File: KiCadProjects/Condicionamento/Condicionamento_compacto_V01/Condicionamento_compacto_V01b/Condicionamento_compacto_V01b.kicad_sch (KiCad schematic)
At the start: 19 parts, among them J1 Entrada, J2 Canais, J3 Conn_01x02, J4 Conn_01x02, U1-Cond1 AD8056ARMZ

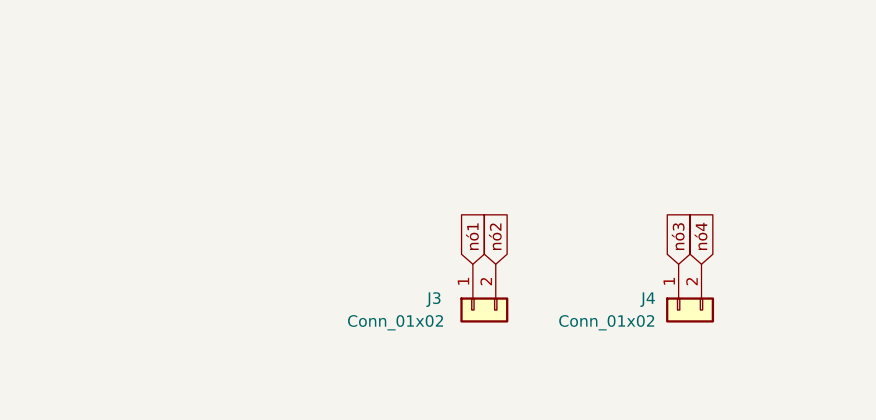
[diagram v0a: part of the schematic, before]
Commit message: V01aCopia: menor, com vias. V01a: maior, sem vias
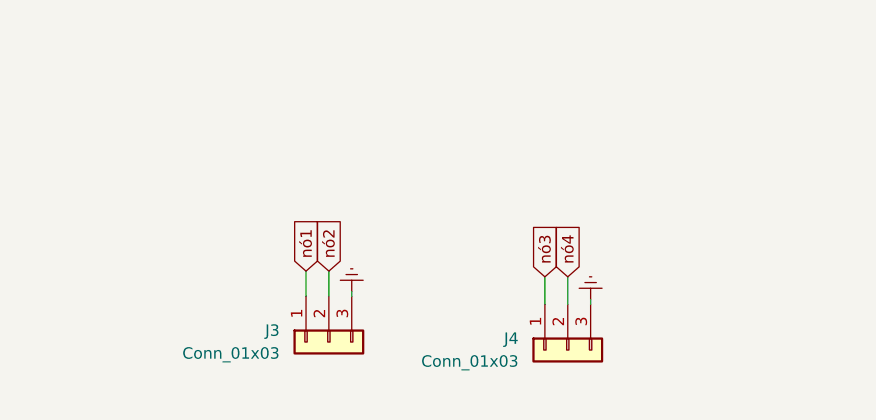
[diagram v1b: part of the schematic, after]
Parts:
- removed J3, J4: Conn_01x02, Connector_PinHeader_2.54mm:PinHeader_1x02_P2.54mm_Vertical, symbol Connector_Generic:Conn_01x02
- added J3, J4: Conn_01x03, Connector_PinHeader_2.54mm:PinHeader_1x03_P2.54mm_Vertical, symbol Connector_Generic:Conn_01x03
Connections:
- net Earth: now also J3.3 (Pin_3), J4.3 (Pin_3)
- net nó1: now also J3.1 (Pin_1)
- net nó2: now also J3.2 (Pin_2)
- net nó3: now also J4.1 (Pin_1)
- net nó4: now also J4.2 (Pin_2)
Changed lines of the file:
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@@
+    (stroke (width 0) (type default))
+  )
+  (wire (pts (xy 128.778 125.222) (xy 128.778 128.016))
     (stroke (width 0) (type default))
   )
@@
     (stroke (width 0) (type default))
   )
+  (wire (pts (xy 155.321 125.857) (xy 155.321 128.905))
+    (stroke (width 0) (type default))
+  )
   (wire (pts (xy 56.134 54.61) (xy 56.134 56.896))
     (stroke (width 0) (type default))
@@
     (stroke (width 0) (type default))
   )
+  (wire (pts (xy 152.781 125.857) (xy 152.781 128.905))
+    (stroke (width 0) (type default))
+  )
+  (wire (pts (xy 131.318 127.508) (xy 131.318 128.016))
+    (stroke (width 0) (type default))
+  )
   (wire (pts (xy 191.77 45.72) (xy 191.77 57.15))
     (stroke (width 0) (type default))
@@
     (stroke (width 0) (type default))
   )
+  (wire (pts (xy 126.238 125.222) (xy 126.238 128.016))
+    (stroke (width 0) (type default))
+  )
   (wire (pts (xy 96.52 54.61) (xy 96.52 65.532))
     (stroke (width 0) (type default))
@@
     (stroke (width 0) (type default))
   )
+  (wire (pts (xy 157.861 128.397) (xy 157.861 128.905))
+    (stroke (width 0) (type default))
+  )
   (wire (pts (xy 99.06 54.61) (xy 96.52 54.61))
     (stroke (width 0) (type default))
@@
     )
   )
+  (global_label "nó4" (shape input) (at 155.321 125.857 90) (fields_autoplaced)
+    (effects (font (size 1.27 1.27)) (justify left))
+    (property "Intersheetrefs" "${INTERSHEET_REFS}" (at 155.321 119.3643 90)
+      (effects (font (size 1.27 1.27)) (justify left) hide)
+    )
+  )
   (global_label "Vref" (shape input) (at 256.54 33.02 90) (fields_autoplaced)
     (effects (font (size 1.27 1.27)) (justify left))
@@
     )
   )
-  (global_label "nó2" (shape input) (at 147.32 124.46 90) (fields_autoplaced)
-    (effects (font (size 1.27 1.27)) (justify left))
-    (property "Intersheetrefs" "${INTERSHEET_REFS}" (at 147.32 117.9673 90)
-      (effects (font (size 1.27 1.27)) (justify left) hide)
-    )
-  )
-  (global_label "nó4" (shape input) (at 170.18 124.46 90) (fields_autoplaced)
-    (effects (font (size 1.27 1.27)) (justify left))
-    (property "Intersheetrefs" "${INTERSHEET_REFS}" (at 170.18 117.9673 90)
+  (global_label "nó1" (shape input) (at 126.238 125.222 90) (fields_autoplaced)
+    (effects (font (size 1.27 1.27)) (justify left))
+    (property "Intersheetrefs" "${INTERSHEET_REFS}" (at 126.238 118.7293 90)
       (effects (font (size 1.27 1.27)) (justify left) hide)
     )
@@
     )
   )
-  (global_label "nó1" (shape input) (at 144.78 124.46 90) (fields_autoplaced)
-    (effects (font (size 1.27 1.27)) (justify left))
-    (property "Intersheetrefs" "${INTERSHEET_REFS}" (at 144.78 117.9673 90)
-      (effects (font (size 1.27 1.27)) (justify left) hide)
-    )
-  )
   (global_label "Vref" (shape input) (at 204.47 33.02 90) (fields_autoplaced)
     (effects (font (size 1.27 1.27)) (justify left))
     (property "Intersheetrefs" "${INTERSHEET_REFS}" (at 204.47 26.4251 90)
+      (effects (font (size 1.27 1.27)) (justify left) hide)
+    )
+  )
+  (global_label "nó2" (shape input) (at 128.778 125.222 90) (fields_autoplaced)
+    (effects (font (size 1.27 1.27)) (justify left))
+    (property "Intersheetrefs" "${INTERSHEET_REFS}" (at 128.778 118.7293 90)
       (effects (font (size 1.27 1.27)) (justify left) hide)
     )
@@
     )
   )
+  (global_label "nó3" (shape input) (at 152.781 125.857 90) (fields_autoplaced)
+    (effects (font (size 1.27 1.27)) (justify left))
+    (property "Intersheetrefs" "${INTERSHEET_REFS}" (at 152.781 119.3643 90)
+      (effects (font (size 1.27 1.27)) (justify left) hide)
+    )
+  )
   (global_label "nó3" (shape input) (at 191.77 45.72 0) (fields_autoplaced)
     (effects (font (size 1.27 1.27)) (justify left))
     (property "Intersheetrefs" "${INTERSHEET_REFS}" (at 198.1833 45.72 0)
-      (effects (font (size 1.27 1.27)) (justify left) hide)
-    )
-  )
-  (global_label "nó3" (shape input) (at 167.64 124.46 90) (fields_autoplaced)
-    (effects (font (size 1.27 1.27)) (justify left))
-    (property "Intersheetrefs" "${INTERSHEET_REFS}" (at 167.64 117.9673 90)
       (effects (font (size 1.27 1.27)) (justify left) hide)
     )
@@
     )
   )
+  (symbol (lib_id "Connector_Generic:Conn_01x03") (at 128.778 133.096 90) (mirror x) (unit 1)
+    (in_bom yes) (on_board yes) (dnp no)
+    (property "Reference" "J3" (at 123.317 131.826 90)
+      (effects (font (size 1.27 1.27)) (justify left))
+    )
+    (property "Value" "Conn_01x03" (at 123.317 134.366 90)
+      (effects (font (size 1.27 1.27)) (justify left))
+    )
+    (property "Footprint" "Connector_PinHeader_2.54mm:PinHeader_1x03_P2.54mm_Vertical" (at 128.778 133.096 0)
+      (effects (font (size 1.27 1.27)) hide)
+    )
+    (property "Datasheet" "~" (at 128.778 133.096 0)
+      (effects (font (size 1.27 1.27)) hide)
+    )
+    (pin "1")
+    (pin "2")
+    (pin "3")
+    (instances
+      (project "Condicionamento_compacto_V01b"
+        (path "/ca05a78d-0094-4531-91c3-e609c3923191"
+          (reference "J3") (unit 1)
+        )
+      )
+    )
+  )
   (symbol (lib_id "power:-9V") (at 129.54 74.93 180) (unit 1)
     (in_bom yes) (on_board yes) (dnp no) (fields_autoplaced)
@@
         (path "/ca05a78d-0094-4531-91c3-e609c3923191"
           (reference "R4") (unit 1)
+        )
+      )
+    )
+  )
+  (symbol (lib_id "power:Earth") (at 157.861 128.397 180) (unit 1)
+    (in_bom yes) (on_board yes) (dnp no) (fields_autoplaced)
+    (property "Reference" "#PWR02" (at 157.861 122.047 0)
+      (effects (font (size 1.27 1.27)) hide)
+    )
+    (property "Value" "Earth" (at 157.861 124.587 0)
+      (effects (font (size 1.27 1.27)) hide)
+    )
+    (property "Footprint" "" (at 157.861 128.397 0)
+      (effects (font (size 1.27 1.27)) hide)
+    )
+    (property "Datasheet" "~" (at 157.861 128.397 0)
+      (effects (font (size 1.27 1.27)) hide)
+    )
+    (pin "1")
+    (instances
+      (project "Condicionamento_compacto_V01b"
+        (path "/ca05a78d-0094-4531-91c3-e609c3923191"
+          (reference "#PWR02") (unit 1)
         )
       )
@@
     )
   )
-  (symbol (lib_id "Connector_Generic:Conn_01x02") (at 167.64 129.54 90) (mirror x) (unit 1)
-    (in_bom yes) (on_board yes) (dnp no) (fields_autoplaced)
-    (property "Reference" "J4" (at 165.1 128.27 90)
-      (effects (font (size 1.27 1.27)) (justify left))
-    )
-    (property "Value" "Conn_01x02" (at 165.1 130.81 90)
-      (effects (font (size 1.27 1.27)) (justify left))
-    )
-    (property "Footprint" "Connector_PinHeader_2.54mm:PinHeader_1x02_P2.54mm_Vertical" (at 167.64 129.54 0)
-      (effects (font (size 1.27 1.27)) hide)
-    )
-    (property "Datasheet" "~" (at 167.64 129.54 0)
-      (effects (font (size 1.27 1.27)) hide)
-    )
-    (pin "1")
-    (pin "2")
-    (instances
-      (project "Condicionamento_compacto_V01b"
-        (path "/ca05a78d-0094-4531-91c3-e609c3923191"
-          (reference "J4") (unit 1)
-        )
-      )
-    )
-  )
   (symbol (lib_id "Device:R") (at 236.22 57.15 90) (unit 1)
     (in_bom yes) (on_board yes) (dnp no) (fields_autoplaced)
@@
     )
   )
-  (symbol (lib_id "Connector_Generic:Conn_01x02") (at 144.78 129.54 90) (mirror x) (unit 1)
-    (in_bom yes) (on_board yes) (dnp no)
-    (property "Reference" "J3" (at 139.7 128.27 90)
-      (effects (font (size 1.27 1.27)) (justify right))
-    )
-    (property "Value" "Conn_01x02" (at 130.81 130.81 90)
-      (effects (font (size 1.27 1.27)) (justify right))
-    )
-    (property "Footprint" "Connector_PinHeader_2.54mm:PinHeader_1x02_P2.54mm_Vertical" (at 144.78 129.54 0)
-      (effects (font (size 1.27 1.27)) hide)
-    )
-    (property "Datasheet" "~" (at 144.78 129.54 0)
-      (effects (font (size 1.27 1.27)) hide)
-    )
-    (pin "2")
-    (pin "1")
-    (instances
-      (project "Condicionamento_compacto_V01b"
-        (path "/ca05a78d-0094-4531-91c3-e609c3923191"
-          (reference "J3") (unit 1)
-        )
-      )
-    )
-  )
   (symbol (lib_id "Device:C_Polarized_Small_US") (at 56.134 59.436 0) (mirror y) (unit 1)
     (in_bom yes) (on_board yes) (dnp no) (fields_autoplaced)
@@
         (path "/ca05a78d-0094-4531-91c3-e609c3923191"
           (reference "C1") (unit 1)
+        )
+      )
+    )
+  )
+  (symbol (lib_id "Connector_Generic:Conn_01x03") (at 155.321 133.985 90) (mirror x) (unit 1)
+    (in_bom yes) (on_board yes) (dnp no)
+    (property "Reference" "J4" (at 149.86 132.715 90)
+      (effects (font (size 1.27 1.27)) (justify left))
+    )
+    (property "Value" "Conn_01x03" (at 149.86 135.255 90)
+      (effects (font (size 1.27 1.27)) (justify left))
+    )
+    (property "Footprint" "Connector_PinHeader_2.54mm:PinHeader_1x03_P2.54mm_Vertical" (at 155.321 133.985 0)
+      (effects (font (size 1.27 1.27)) hide)
+    )
+    (property "Datasheet" "~" (at 155.321 133.985 0)
+      (effects (font (size 1.27 1.27)) hide)
+    )
+    (pin "1")
+    (pin "2")
+    (pin "3")
+    (instances
+      (project "Condicionamento_compacto_V01b"
+        (path "/ca05a78d-0094-4531-91c3-e609c3923191"
+          (reference "J4") (unit 1)
         )
       )
@@
         )
       )
+    )
+  )
+  (symbol (lib_id "power:Earth") (at 131.318 127.508 180) (unit 1)
+    (in_bom yes) (on_board yes) (dnp no) (fields_autoplaced)
+    (property "Reference" "#PWR01" (at 131.318 121.158 0)
+      (effects (font (size 1.27 1.27)) hide)
+    )
+    (property "Value" "Earth" (at 131.318 123.698 0)
+      (effects (font (size 1.27 1.27)) hide)
+    )
+    (property "Footprint" "" (at 131.318 127.508 0)
+      (effects (font (size 1.27 1.27)) hide)
+    )
+    (property "Datasheet" "~" (at 131.318 127.508 0)
+      (effects (font (size 1.27 1.27)) hide)
+    )
+    (pin "1")
+    (instances
+      (project "Condicionamento_compacto_V01b"
+        (path "/ca05a78d-0094-4531-91c3-e609c3923191"
+          (reference "#PWR01") (unit 1)
+        )
+      )
